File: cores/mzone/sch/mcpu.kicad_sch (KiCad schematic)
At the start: 45 parts

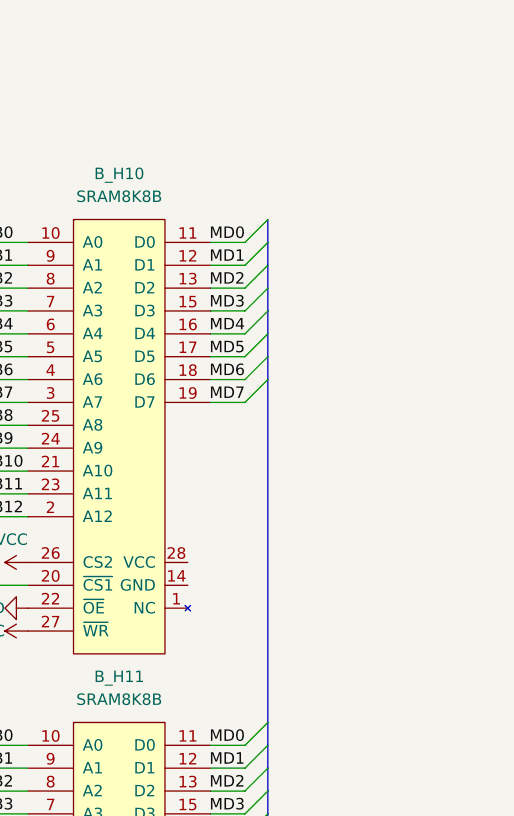
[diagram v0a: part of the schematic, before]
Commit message: mzone core
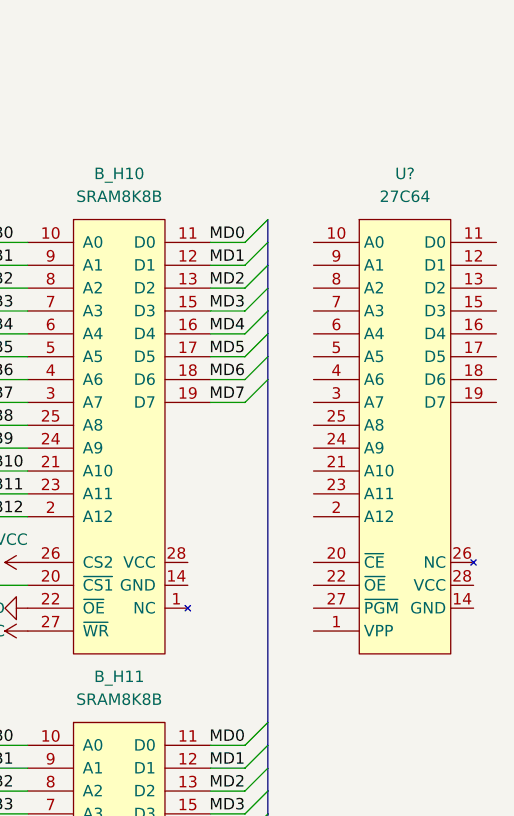
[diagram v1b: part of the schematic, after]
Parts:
- added U?: 27C64, symbol jt_rom:27C64

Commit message: mzone core clean up
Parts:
- removed B_H10, B_H11, B_H12, B_H6, B_H7, B_H8: SRAM8K8B, symbol jt_ram:SRAM8K8B
- added B_H11, B_H12, B_H6, B_H7, B_H8: 27C64, symbol jt_rom:27C64
- gave numbers to parts that had none: 1
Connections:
- net ~{DBGROM}2 is gone; now on net ~{MROM}2: B_B7.11 (O4)
- net AB0: now also B_H9.10 (A0), B_H11.10 (A0), B_H12.10 (A0), B_H6.10 (A0), B_H7.10 (A0), B_H8.10 (A0)
- net AB1: now also B_H9.9 (A1), B_H11.9 (A1), B_H12.9 (A1), B_H6.9 (A1), B_H7.9 (A1), B_H8.9 (A1)
- net AB10: now also B_H9.21 (A10), B_H11.21 (A10), B_H12.21 (A10), B_H6.21 (A10), B_H7.21 (A10), B_H8.21 (A10)
- net AB11: now also B_H9.23 (A11), B_H11.23 (A11), B_H12.23 (A11), B_H6.23 (A11), B_H7.23 (A11), B_H8.23 (A11)
- net AB12: now also B_H9.2 (A12), B_H11.2 (A12), B_H12.2 (A12), B_H6.2 (A12), B_H7.2 (A12), B_H8.2 (A12)
- net AB2: now also B_H9.8 (A2), B_H11.8 (A2), B_H12.8 (A2), B_H6.8 (A2), B_H7.8 (A2), B_H8.8 (A2)
- net AB3: now also B_H9.7 (A3), B_H11.7 (A3), B_H12.7 (A3), B_H6.7 (A3), B_H7.7 (A3), B_H8.7 (A3)
- net AB4: now also B_H9.6 (A4), B_H11.6 (A4), B_H12.6 (A4), B_H6.6 (A4), B_H7.6 (A4), B_H8.6 (A4)
- net AB5: now also B_H9.5 (A5), B_H11.5 (A5), B_H12.5 (A5), B_H6.5 (A5), B_H7.5 (A5), B_H8.5 (A5)
- net AB6: now also B_H9.4 (A6), B_H11.4 (A6), B_H12.4 (A6), B_H6.4 (A6), B_H7.4 (A6), B_H8.4 (A6)
- net AB7: now also B_H9.3 (A7), B_H11.3 (A7), B_H12.3 (A7), B_H6.3 (A7), B_H7.3 (A7), B_H8.3 (A7)
- net AB8: now also B_H9.25 (A8), B_H11.25 (A8), B_H12.25 (A8), B_H6.25 (A8), B_H7.25 (A8), B_H8.25 (A8)
- net AB9: now also B_H9.24 (A9), B_H11.24 (A9), B_H12.24 (A9), B_H6.24 (A9), B_H7.24 (A9), B_H8.24 (A9)
- net GND: now also B_H9.27 (~{PGM}), B_H11.27 (~{PGM}), B_H12.27 (~{PGM}), B_H6.27 (~{PGM}), B_H7.27 (~{PGM}), B_H8.27 (~{PGM})
- net MD0: now also B_H9.11 (D0), B_H11.11 (D0), B_H12.11 (D0), B_H6.11 (D0), B_H7.11 (D0), B_H8.11 (D0)
- net MD1: now also B_H9.12 (D1), B_H11.12 (D1), B_H12.12 (D1), B_H6.12 (D1), B_H7.12 (D1), B_H8.12 (D1)
- net MD2: now also B_H9.13 (D2), B_H11.13 (D2), B_H12.13 (D2), B_H6.13 (D2), B_H7.13 (D2), B_H8.13 (D2)
- net MD3: now also B_H9.15 (D3), B_H11.15 (D3), B_H12.15 (D3), B_H6.15 (D3), B_H7.15 (D3), B_H8.15 (D3)
- net MD4: now also B_H9.16 (D4), B_H11.16 (D4), B_H12.16 (D4), B_H6.16 (D4), B_H7.16 (D4), B_H8.16 (D4)
- net MD5: now also B_H9.17 (D5), B_H11.17 (D5), B_H12.17 (D5), B_H6.17 (D5), B_H7.17 (D5), B_H8.17 (D5)
- net MD6: now also B_H9.18 (D6), B_H11.18 (D6), B_H12.18 (D6), B_H6.18 (D6), B_H7.18 (D6), B_H8.18 (D6)
- net MD7: now also B_H9.19 (D7), B_H11.19 (D7), B_H12.19 (D7), B_H6.19 (D7), B_H7.19 (D7), B_H8.19 (D7)
- net VCC: now also B_H9.1 (VPP), B_H9.20 (~{CE}), B_H11.1 (VPP), B_H11.20 (~{CE}), B_H12.1 (VPP), B_H12.20 (~{CE}), B_H6.1 (VPP), B_H6.20 (~{CE}), B_H7.1 (VPP), B_H7.20 (~{CE}), B_H8.1 (VPP), B_H8.20 (~{CE})
- net ~{MROM}2: now reaches B_H9.22 (~{OE})
- net INT renamed INTSND
- net INT' renamed INTSND'
- net ~{DBGROM}0 renamed ~{MROM}0
- net ~{MROM}0: now also B_H12.22 (~{OE})
- net ~{DBGROM}1 renamed ~{MROM}1
- net ~{MROM}1: now also B_H11.22 (~{OE})
- net ~{DBGROM}3 renamed ~{MROM}3
- net ~{MROM}3: now also B_H8.22 (~{OE})
- net ~{DBGROM}4 renamed ~{MROM}4
- net ~{MROM}4: now also B_H7.22 (~{OE})
- net ~{DBGROM}5 renamed ~{MROM}5
- net ~{MROM}5: now also B_H6.22 (~{OE})
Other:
- note added: "Called INT in original schematics."
- moved on the sheet: B_B12A, B_B12D, B_B13A, B_B13B, B_H9

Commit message: mzone core sch
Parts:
- removed B_FG14: 74LS240, symbol jt74:74LS240
- renumbered B_C1 to B_C12, G13 to B_G13
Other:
- note removed: "check if it is pin 17 ? , var ska det här vara?"
- note removed: "says pin16 in sch, not 6."

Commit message: mzone core sch
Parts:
- removed A11: 74LS04, symbol jt74:74LS04
- removed AR6: R_Network04, Resistor_THT:R_Array_SIP5, symbol Device:R_Network04
- removed unit 2 of B_B12
- removed unit 3 of B_B12
- removed B_B7: 74LS138, symbol jt74:74LS138
- removed B_C11: 74LS08, symbol jt74:74LS08
- removed B_C9: 74LS74, symbol jt74:74LS74
- removed unit 4 of B_DE11
- removed unit 1 of B_DE11
- removed unit 1 of B_DE12
- removed unit 3 of B_DE9
- removed DE6: 27C64, symbol jt_rom:27C64
- removed U?: Z80, symbol jt_cpu:Z80
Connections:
- no-connect marks 9 -> 7
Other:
- note removed: "KONAMI-1: MA, MB Z80: SA, DB I8039: IA, IB"
